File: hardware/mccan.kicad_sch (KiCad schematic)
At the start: 0 parts

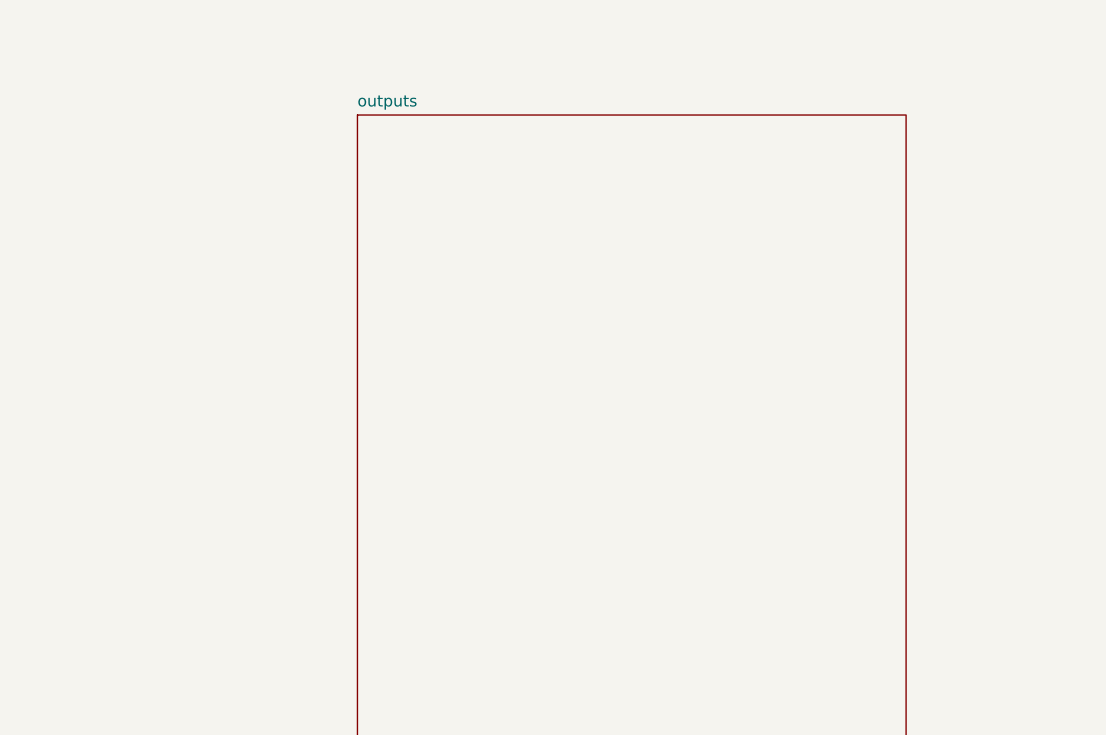
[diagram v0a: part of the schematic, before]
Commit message: hw(sch): outputs sheet - schematic capture complete, ERC clean (Task 6)
PCA9685, 12 RGB switching channels with sense shunts, the 16:1 mux and its
sense-path protection, the dual PROFET, four PTCs and the six panel connectors.
164 symbols.  This completes schematic capture.

The gate the plan sets for this task is met: kicad-cli sch erc --severity-all
--exit-code-violations returns exit=0 with 0 errors and 0 warnings across all
five sheets.  Every unconnected pin is either connected or no-connect flagged.

ChannelIndex order verified from the netlist rather than the drawing, because
getting it wrong silently scrambles colours and corners against firmware that is
already written: LED0->PWM_FL_R through LED11->PWM_RR_B, with FET n and mux
address n lining up with PWM channel n on every one of the twelve.

Three new symbols.  ADG706 and NX5020UNBKS are verified from local datasheets;
the FET is built as a 2-unit symbol so each channel draws as one device and six
packages cover twelve channels.

Two deliberate deviations from the plan, both written up.  ~OE is pulled LOW
rather than high: taken literally the plan would leave the board permanently
dark, since no GPIO is allocated to release it, and "disabled by default" is
already delivered by the switched rail plus the PCA9685's power-on state.  And
the plan's Step 3 still quotes 1 ohm / 140 mV / 2512 shunts, which predate the
RGB load being corrected ~4x downward; the sheet is built to the current 10 ohm
/ 267 mV values.

Surfaces a cross-domain dependency that would otherwise have been lost between
disciplines: the shunt package rating is conditional on FIRMWARE latching a
shorted channel off.  Normal dissipation is 7 mW, but a shorted channel puts
~2.5 W into one shunt - ten times a 1206's rating - survivable only because the
sweep is brief and firmware stops driving it.  Recorded on the sheet, in
part-selection.md, and flagged for the firmware spec.

BLOCKER for Task 8: no Infineon datasheet for the BTS7008-2EPA is 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
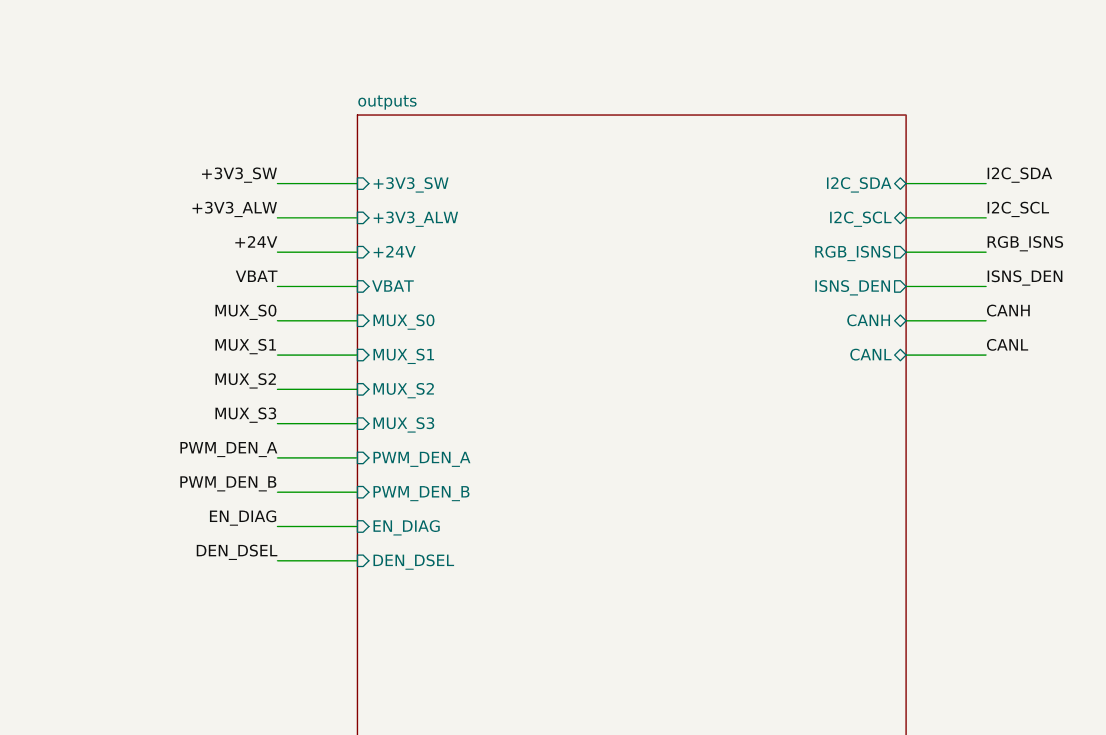
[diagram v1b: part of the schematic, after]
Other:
- sheet outputs ports: added +24V, +3V3_ALW, +3V3_SW, CANH, CANL, DEN_DSEL, EN_DIAG, I2C_SCL, I2C_SDA, ISNS_DEN, MUX_S0, MUX_S1, MUX_S2, MUX_S3, PWM_DEN_A, PWM_DEN_B, RGB_ISNS, VBAT; removed none

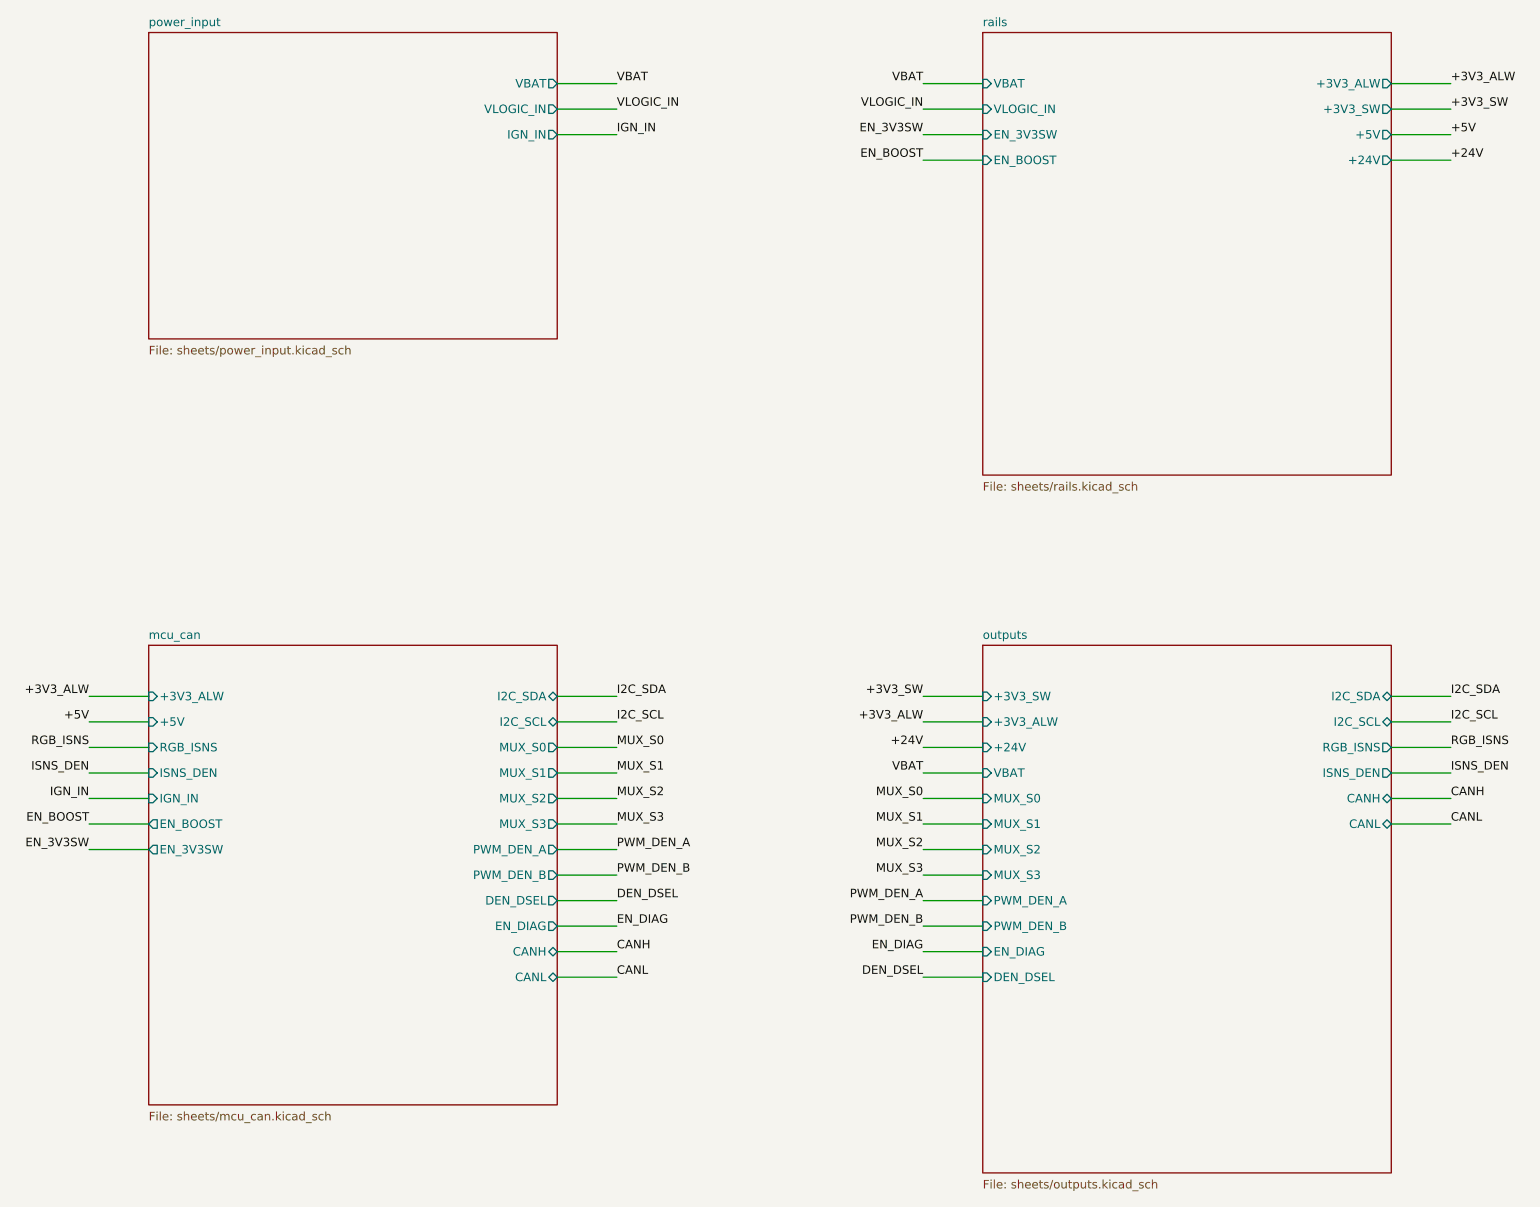
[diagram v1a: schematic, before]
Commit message: hw(root): phase-A hierarchy; ERC clean, every net read
Root sheet pins now match every child hierarchical label (stale plan3 pins
removed; VBAT_B added with a root label and PWR_FLAG; OUT_* x12, DIAG_*_Q,
SNS_A-C, EN_5V, +5V, +3V3_ALW, VBAT, CANH/CANL wired by name).

Also fixed in symlib.py: TPS4H160B_Q1 OUTn pads retyped output -> passive.
Each channel's two pads are one output tied together; two Output pins on a
net raised 10 pin_to_pin errors that are not in the circuit (same treatment
as BTS7008 OUTn). Regenerated outputs sheet and mccan_parts.kicad_sym.

ERC: 0 errors, 0 warnings. check_netlist: all groups PASS. verify_fpmap: 144 ok.
DNP set: R2, R3 (0R links across the choke), R26 (120R CAN termination).

Co-Authored-By: Claude Sonnet 5.5 <noreply@anthropic.com>
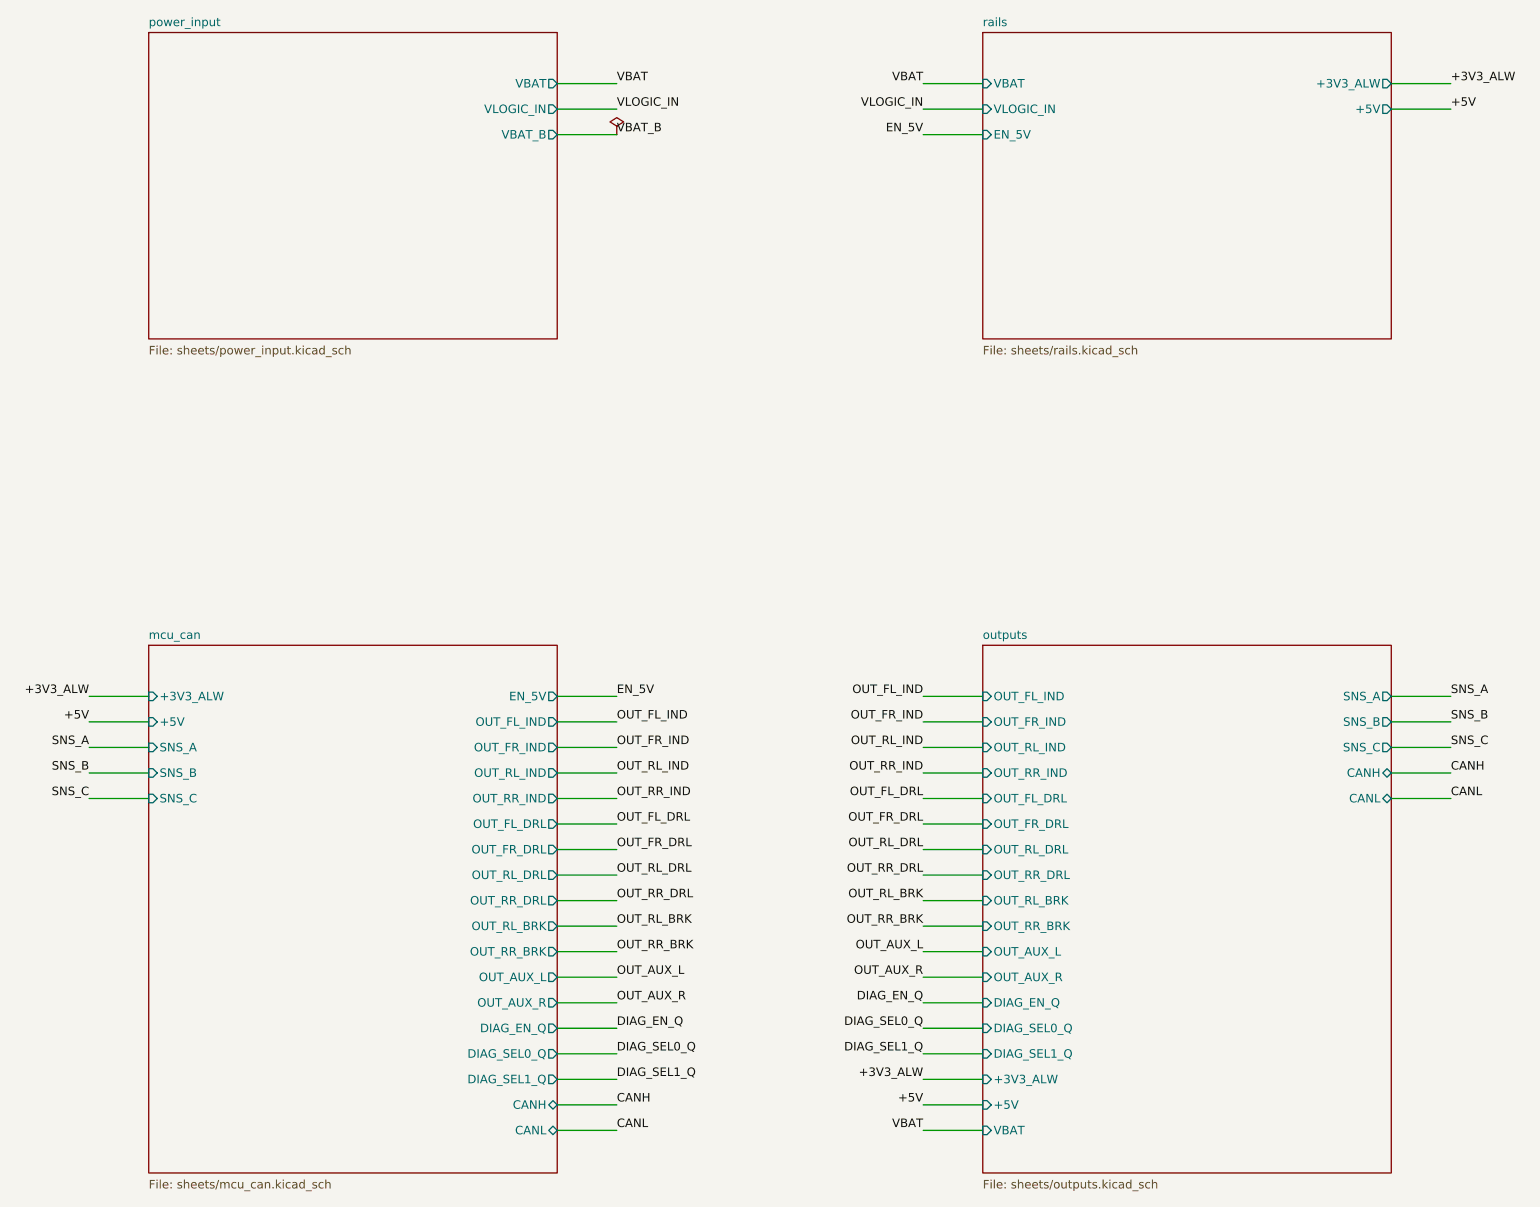
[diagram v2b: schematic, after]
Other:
- sheet mcu_can ports: added DIAG_EN_Q, DIAG_SEL0_Q, DIAG_SEL1_Q, EN_5V, OUT_AUX_L, OUT_AUX_R, OUT_FL_DRL, OUT_FL_IND, OUT_FR_DRL, OUT_FR_IND, OUT_RL_BRK, OUT_RL_DRL, OUT_RL_IND, OUT_RR_BRK, OUT_RR_DRL, OUT_RR_IND, SNS_A, SNS_B, SNS_C; removed DEN_DSEL, EN_3V3SW, EN_BOOST, EN_DIAG, I2C_SCL, I2C_SDA, IGN_IN, ISNS_DEN, MUX_S0, MUX_S1, MUX_S2, MUX_S3, PWM_DEN_A, PWM_DEN_B, RGB_ISNS
- sheet outputs ports: added +5V, DIAG_EN_Q, DIAG_SEL0_Q, DIAG_SEL1_Q, OUT_AUX_L, OUT_AUX_R, OUT_FL_DRL, OUT_FL_IND, OUT_FR_DRL, OUT_FR_IND, OUT_RL_BRK, OUT_RL_DRL, OUT_RL_IND, OUT_RR_BRK, OUT_RR_DRL, OUT_RR_IND, SNS_A, SNS_B, SNS_C; removed +24V, +3V3_SW, DEN_DSEL, EN_DIAG, I2C_SCL, I2C_SDA, ISNS_DEN, MUX_S0, MUX_S1, MUX_S2, MUX_S3, PWM_DEN_A, PWM_DEN_B, RGB_ISNS
- sheet power_input ports: added VBAT_B; removed IGN_IN
- sheet rails ports: added EN_5V; removed +24V, +3V3_SW, EN_3V3SW, EN_BOOST
